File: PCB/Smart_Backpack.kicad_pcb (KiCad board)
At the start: 2 copper layers, 58 parts, among them J1 Conn_01x03_Pin, J2 Conn_01x02_Pin, J3 Conn_01x02_Pin, J4 Conn_01x03_Pin, J5 Conn_01x03_Pin, J6 Conn_01x03_Pin, J7 Conn_01x07_Pin, J8 Conn_01x08_Socket, J9 USB_C_Receptacle_USB2.0_16P, SW1 SW_Push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

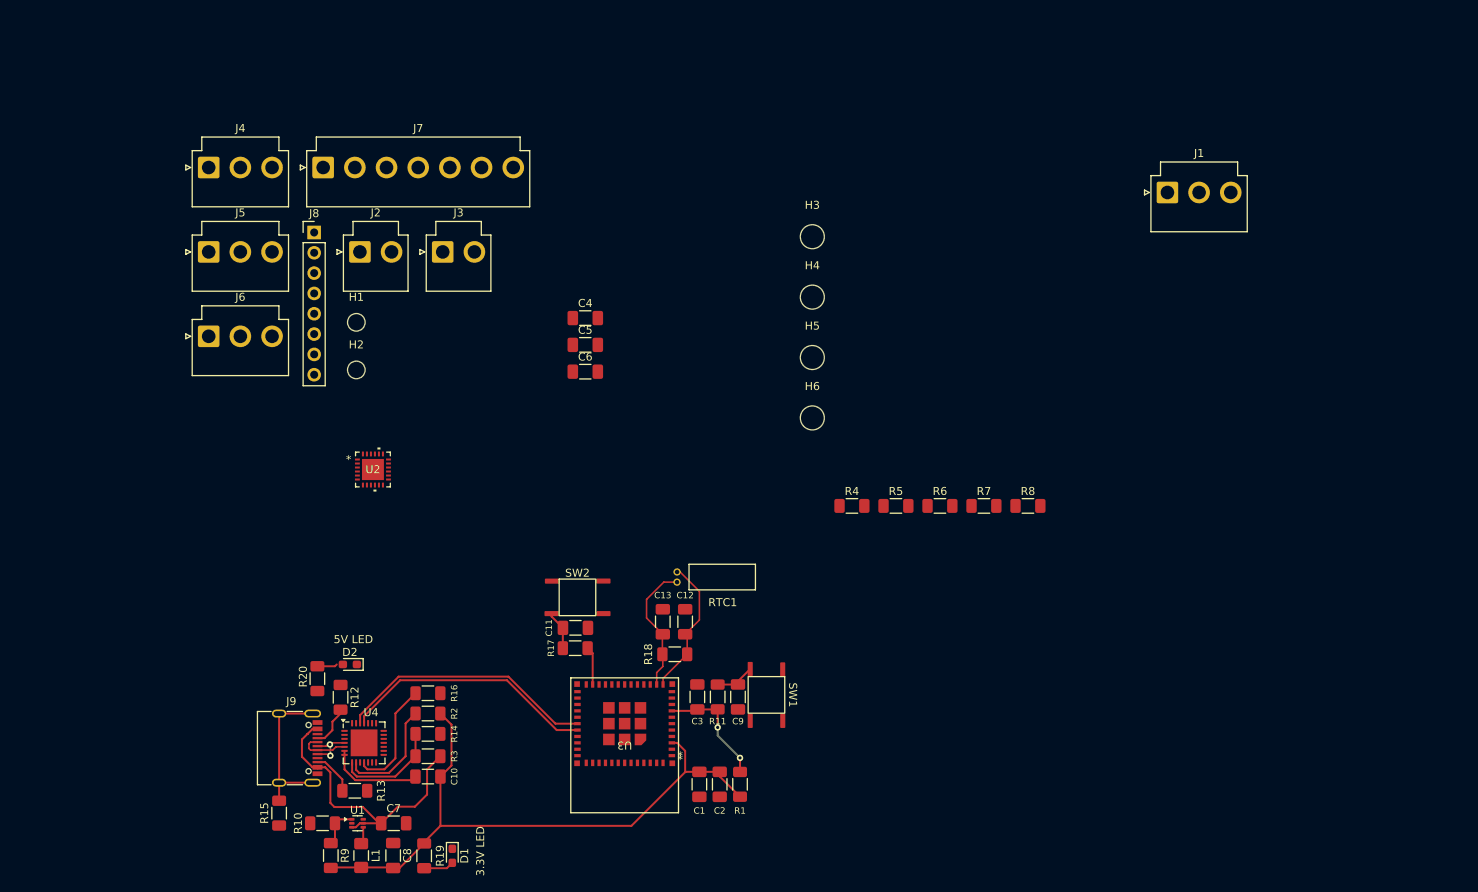
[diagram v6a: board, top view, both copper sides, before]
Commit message: route IMU, fix MCU orientation, space GPS mounting
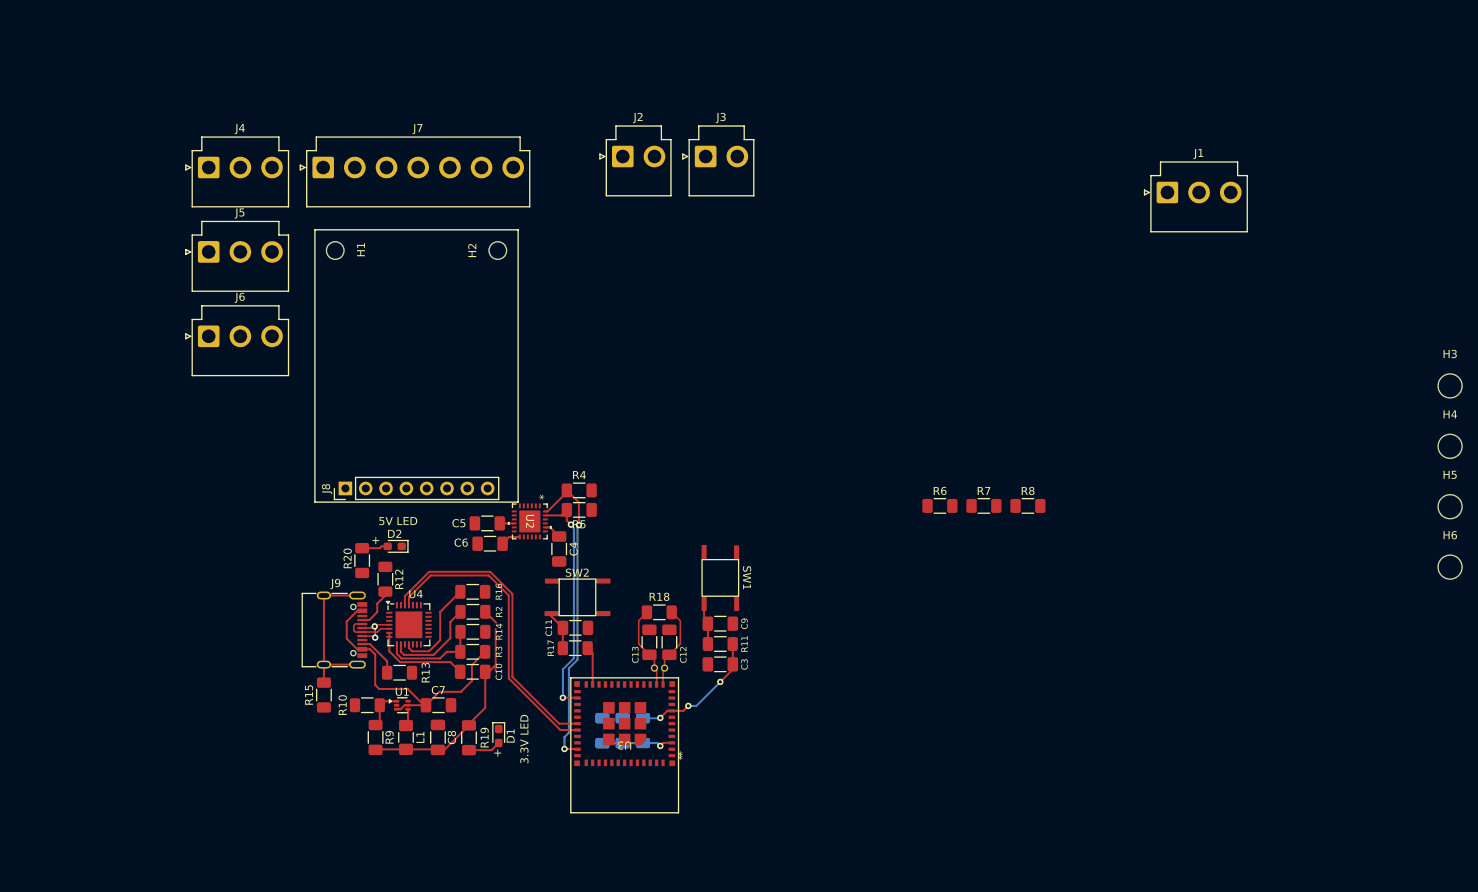
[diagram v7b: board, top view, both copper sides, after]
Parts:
- C1, C2, R1, RTC1: moved to B.Cu
- moved H3 81.9 mm to (229.2, 64.5)
- moved H4 81.9 mm to (229.2, 72.0)
- moved H5 81.9 mm to (229.2, 79.6)
- moved H6 81.9 mm to (229.2, 87.2)
- moved R5 39.6 mm to (120.4, 80.0), turned to 180 degrees
- moved J2 35.0 mm to (125.8, 35.8)
- moved J3 35.0 mm to (136.2, 35.8)
- moved R4 34.1 mm to (120.4, 77.6), turned to 180 degrees
- moved J8 32.2 mm to (91.1, 77.3), turned to 90 degrees
- moved C4 29.1 mm to (117.9, 84.9), turned to -90 degrees
- moved C5 25.5 mm to (108.9, 81.7), turned to 180 degrees
- moved C6 24.6 mm to (109.2, 84.2), turned to 180 degrees
- moved H2 23.1 mm to (110.2, 47.6), turned to 90 degrees
- moved U2 20.7 mm to (114.2, 81.4), turned to -90 degrees
- moved D1 16.1 mm to (110.3, 108.3)
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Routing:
- net IMU_SDA: track 0.00 -> 39.2 mm, vias 0 -> 2
- net +3V3: track 77.7 -> 40.5 mm, vias 0 -> 1
- net IMU_SCL: track 0.00 -> 29.2 mm, vias 0 -> 2
- net RTC_XP: track 17.5 -> 10.3 mm
- net RTC_XN: track 16.5 -> 10.4 mm
- net Flash_RXD: track 32.0 -> 37.3 mm
- net Flash_TXD: track 32.6 -> 37.9 mm
- net Net-(U2-CPOUT): track 0.00 -> 2.20 mm
- net ESP_EN: track 14.8 -> 17.0 mm, vias 2 -> 3
- net Net-(U4-~{SUSPEND}): track 14.3 -> 12.2 mm
- net Net-(U4-~{RST}): track 14.0 -> 11.9 mm
- net Net-(U2-REGOUT): track 0.00 -> 1.80 mm
- net +5V: track 37.2 -> 35.9 mm
- net Net-(U4-VBUS): track 13.2 -> 12.2 mm
- net Net-(D2-A): track 2.52 -> 3.28 mm
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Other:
- board text added: "+"

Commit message: place and route connectors, add edges
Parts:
- removed H6: MountingHole, MountingHole:MountingHole_3mm
- J1, J4, J5, J6: footprint Connector_JST:JST_VH_B3P-VH_1x03_P3.96mm_Vertical -> Connector_JST:JST_VH_B3PS-VH_1x03_P3.96mm_Horizontal
- J2, J3: footprint Connector_JST:JST_VH_B2P-VH_1x02_P3.96mm_Vertical -> Connector_JST:JST_VH_B2PS-VH_1x02_P3.96mm_Horizontal
- J7: footprint Connector_JST:JST_VH_B7P-VH_1x07_P3.96mm_Vertical -> Connector_JST:JST_VH_B7PS-VH_1x07_P3.96mm_Horizontal
- moved H5 142.6 mm to (89.8, 109.5)
- moved H3 140.9 mm to (89.8, 44.1)
- moved J1 89.5 mm to (104.7, 48.6), turned to 180 degrees
- moved H4 87.3 mm to (146.5, 44.1)
- moved J5 74.7 mm to (141.7, 79.3), turned to 90 degrees
- moved J6 68.0 mm to (141.7, 64.8), turned to 90 degrees
- moved R8 52.1 mm to (129.7, 56.5)
- moved J4 46.3 mm to (118.9, 48.6), turned to 180 degrees
- moved R7 43.9 mm to (132.1, 59.1)
- moved R6 35.7 mm to (134.5, 61.8)
- moved C6 24.4 mm to (133.6, 85.8), turned to -90 degrees
- moved C5 22.6 mm to (131.1, 86.2), turned to -90 degrees
- moved J7 19.1 mm to (94.9, 55.1), turned to -90 degrees
- moved J2 18.6 mm to (139.4, 48.6), turned to 180 degrees
- moved C4 17.5 mm to (132.1, 74.7), turned to 90 degrees
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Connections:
- J7 pad 2: RFID_CS -> RFID_RST
- J7 pad 4: RFID_MOSI -> RFID_MISO
- J7 pad 5: RFID_MISO -> RFID_MOSI
- J7 pad 6: RFID_RST -> RFID_CS
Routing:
- net MOIST_SIG: track 0.00 -> 68.3 mm
- net LAPTOP: track 0.00 -> 64.7 mm
- net FLEX_1: track 0.00 -> 64.7 mm
- net FLEX_2: track 0.00 -> 61.8 mm
- net RFID_RST: track 0.00 -> 58.8 mm
- net RFID_SCLK: track 0.00 -> 56.5 mm
- net RFID_MISO: track 0.00 -> 54.4 mm
- net RFID_MOSI: track 0.00 -> 52.3 mm
- net HALL_2: track 0.00 -> 51.1 mm
- net RFID_CS: track 0.00 -> 50.3 mm
- net HALL_1: track 0.00 -> 37.3 mm
- net GPS_RX: track 0.00 -> 30.1 mm
- net GPS_TX: track 0.00 -> 23.6 mm
- net ESP_EN: track 17.0 -> 24.7 mm, vias 3 -> 2
- net +5V: track 35.9 -> 42.0 mm
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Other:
- board outline added: 65.8 x 74.4 mm
- board text added: "This GPS works by memorizing bollards and learning car meta"
